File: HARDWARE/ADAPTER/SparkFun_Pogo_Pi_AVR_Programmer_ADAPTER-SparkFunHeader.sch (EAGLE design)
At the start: 4 parts, among them J2 CABLE

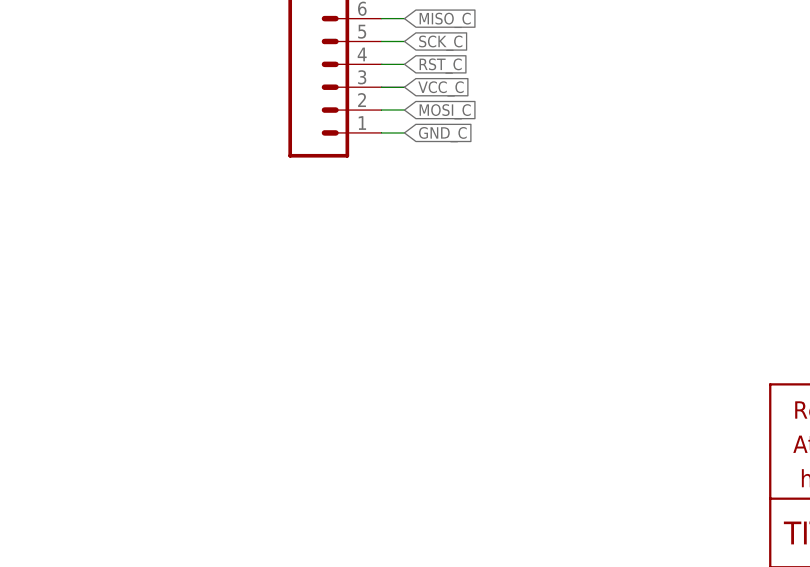
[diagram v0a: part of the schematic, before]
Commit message: Added proper pogo header.
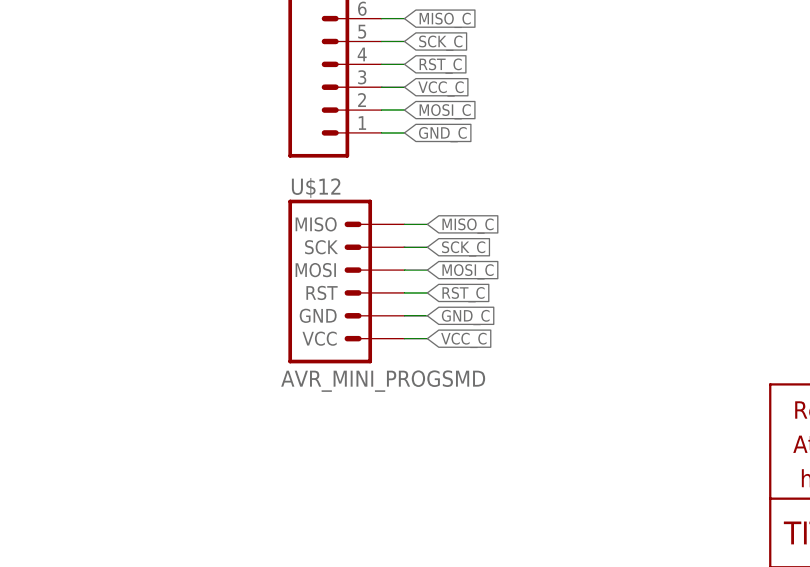
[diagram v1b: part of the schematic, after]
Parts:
- added U$12: AVR_MINI_PROGSMD, SparkFun-Connectors:AVR_MINI_PROGSMD
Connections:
- net GND_C: now also U$12.GND
- net MISO_C: now also U$12.MISO
- net MOSI_C: now also U$12.MOSI
- net RST_C: now also U$12.RST
- net SCK_C: now also U$12.SCK
- net VCC_C: now also U$12.VCC
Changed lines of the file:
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@@
 <part name="LOGO1" library="SparkFun-Aesthetics" deviceset="SFE_LOGO_FLAME" device=".1_INCH"/>
 <part name="JP1" library="SparkFun-Connectors" deviceset="M06" device="POLAR"/>
+<part name="U$12" library="SparkFun-Connectors" deviceset="AVR_MINI_PROG" device="SMD"/>
 </parts>
 <sheets>
@@
 <instance part="LOGO1" gate="G$1" x="228.6" y="220.98"/>
 <instance part="JP1" gate="G$1" x="106.68" y="251.46"/>
+<instance part="U$12" gate="G$1" x="106.68" y="228.6" rot="R180"/>
 </instances>
 <busses>
@@
 <label x="114.3" y="248.92" size="1.27" layer="95" xref="yes"/>
 </segment>
+<segment>
+<pinref part="U$12" gate="G$1" pin="MOSI"/>
+<wire x1="114.3" y1="231.14" x2="116.84" y2="231.14" width="0.1524" layer="91"/>
+<label x="116.84" y="231.14" size="1.27" layer="95" xref="yes"/>
+</segment>
 </net>
 <net name="MISO_C" class="0">
@@
 <wire x1="111.76" y1="259.08" x2="114.3" y2="259.08" width="0.1524" layer="91"/>
 <label x="114.3" y="259.08" size="1.27" layer="95" xref="yes"/>
+</segment>
+<segment>
+<pinref part="U$12" gate="G$1" pin="MISO"/>
+<wire x1="114.3" y1="236.22" x2="116.84" y2="236.22" width="0.1524" layer="91"/>
+<label x="116.84" y="236.22" size="1.27" layer="95" xref="yes"/>
 </segment>
 </net>
@@
 <label x="114.3" y="256.54" size="1.27" layer="95" xref="yes"/>
 </segment>
+<segment>
+<pinref part="U$12" gate="G$1" pin="SCK"/>
+<wire x1="114.3" y1="233.68" x2="116.84" y2="233.68" width="0.1524" layer="91"/>
+<label x="116.84" y="233.68" size="1.27" layer="95" xref="yes"/>
+</segment>
 </net>
 <net name="RST_C" class="0">
@@
 <wire x1="111.76" y1="254" x2="114.3" y2="254" width="0.1524" layer="91"/>
 <label x="114.3" y="254" size="1.27" layer="95" xref="yes"/>
+</segment>
+<segment>
+<pinref part="U$12" gate="G$1" pin="RST"/>
+<wire x1="114.3" y1="228.6" x2="116.84" y2="228.6" width="0.1524" layer="91"/>
+<label x="116.84" y="228.6" size="1.27" layer="95" xref="yes"/>
 </segment>
 </net>
@@
 <label x="114.3" y="246.38" size="1.27" layer="95" xref="yes"/>
 </segment>
+<segment>
+<pinref part="U$12" gate="G$1" pin="GND"/>
+<wire x1="114.3" y1="226.06" x2="116.84" y2="226.06" width="0.1524" layer="91"/>
+<label x="116.84" y="226.06" size="1.27" layer="95" xref="yes"/>
+</segment>
 </net>
 <net name="VCC_C" class="0">
@@
 <label x="114.3" y="251.46" size="1.27" layer="95" xref="yes"/>
 </segment>
+<segment>
+<pinref part="U$12" gate="G$1" pin="VCC"/>
+<wire x1="114.3" y1="223.52" x2="116.84" y2="223.52" width="0.1524" layer="91"/>
+<label x="116.84" y="223.52" size="1.27" layer="95" xref="yes"/>
+</segment>
 </net>
